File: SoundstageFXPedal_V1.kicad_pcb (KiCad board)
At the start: 2 copper layers, 104 x 63 mm, 109 parts, among them J101 JST XH-B4B, J102 Barrel_Jack, J103 BATT_CONN, J202 XLR3, J601 Conn_01x02_Pin, J602 Conn_01x02_Pin, Q301 2N3906, Q302 2N3906, Q401 2N5457, Q701 BC109, Q702 BC109, SW201 SW_DPDT_x2, U301 TL072, U401 TL072, U501 TL072

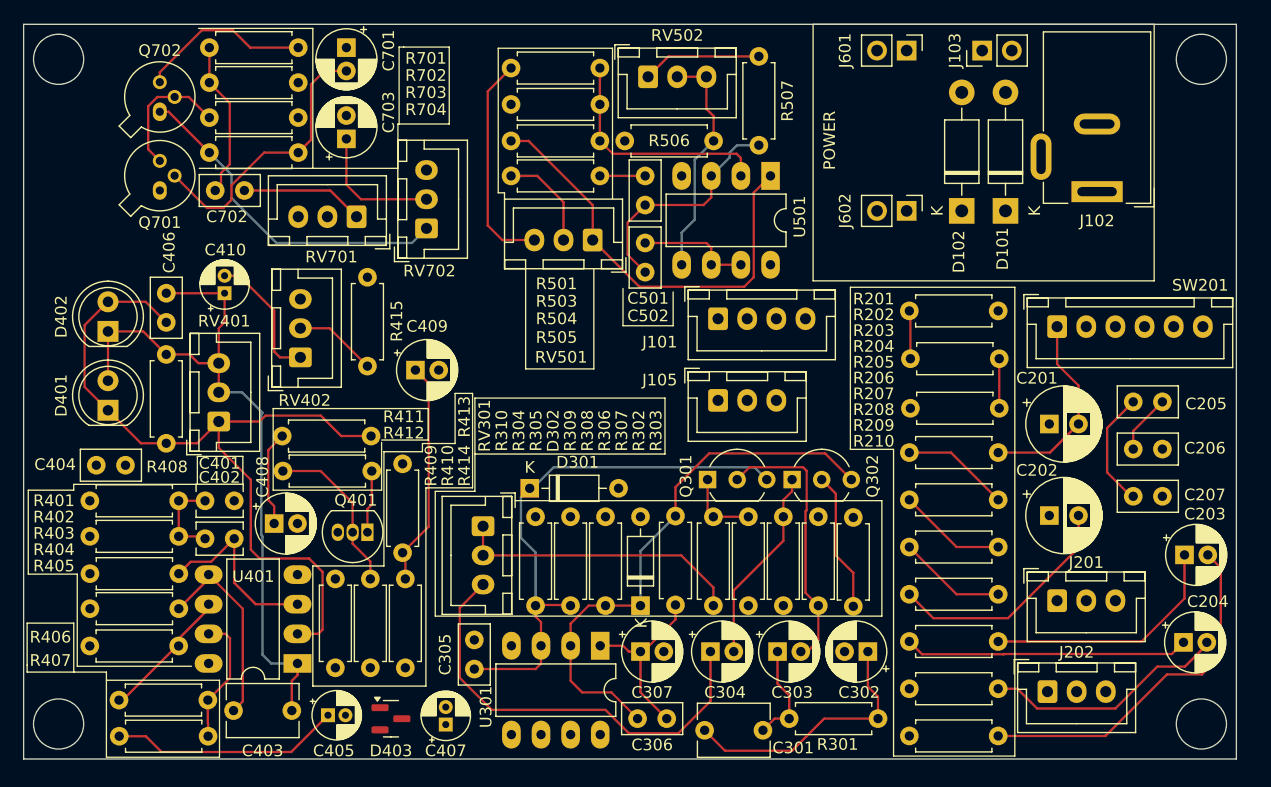
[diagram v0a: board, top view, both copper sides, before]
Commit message: Completed routing, cleanup, and artwork export
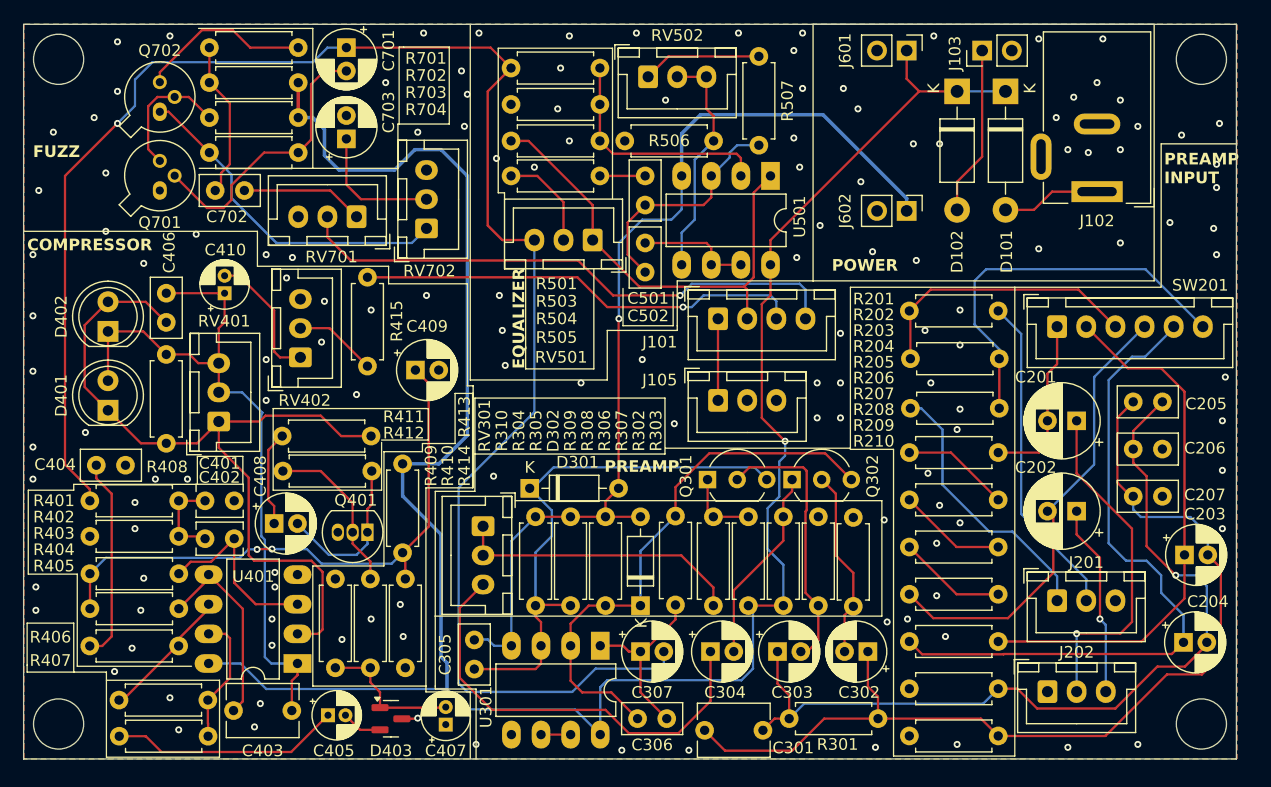
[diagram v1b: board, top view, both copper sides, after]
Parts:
- moved D102 10.3 mm to (135.8, 130.0), turned to -90 degrees
- moved D101 10.2 mm to (139.9, 130.0), turned to -90 degrees
- moved C202 2.37 mm to (146.0, 166.0), turned to 180 degrees
- moved C201 2.36 mm to (146.0, 158.2), turned to 180 degrees
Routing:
- net VCC: track 0.00 -> 197.6 mm, vias 0 -> 1
- net COMP_IN: track 18.8 -> 153.1 mm, vias 0 -> 1
- net VEE: track 0.00 -> 85.4 mm, vias 0 -> 1
- net FUZZ_OUT: track 0.00 -> 47.9 mm, vias 0 -> 1
- net PREAMP_IN_N: track 35.0 -> 74.2 mm, vias 0 -> 1
- net COMP_OUT: track 0.00 -> 38.2 mm, vias 0 -> 1
- net Net-(SW201B-B): track 24.4 -> 58.1 mm
- net /Compressor/VBIAS: track 19.4 -> 51.0 mm, vias 0 -> 2
- net Net-(SW201B-C): track 4.25 -> 33.8 mm
- net Net-(C201-Pad1): track 0.00 -> 29.4 mm, vias 0 -> 1
- net Net-(J201-Pad2): track 0.00 -> 28.0 mm
- net Net-(SW201A-B): track 21.2 -> 46.0 mm
- net Net-(J201-Pad1): track 0.00 -> 23.4 mm
- net PREAMP_IN_P: track 64.0 -> 84.3 mm
- net Net-(SW201A-C): track 4.14 -> 23.9 mm
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- added copper zone on B.Cu, net GND
- added copper zone on F.Cu, net GND
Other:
- board text added: "COMPRESSOR"
- board text added: "EQUALIZER"
- board text added: "FUZZ"
- board text added: "PREAMP"
- board text added: "PREAMP INPUT"
- board text added: "Schulich Soundstage Audio Design Workshop FX PCB V1, 2024"
